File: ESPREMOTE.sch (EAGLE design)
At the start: 37 parts, among them IC1 ESP12SMT, IC2 LD111733, J1 DC_2_1MM, Q1 2N7002, Q2 2N7002, Q3 2N7002, Q4 2N7002

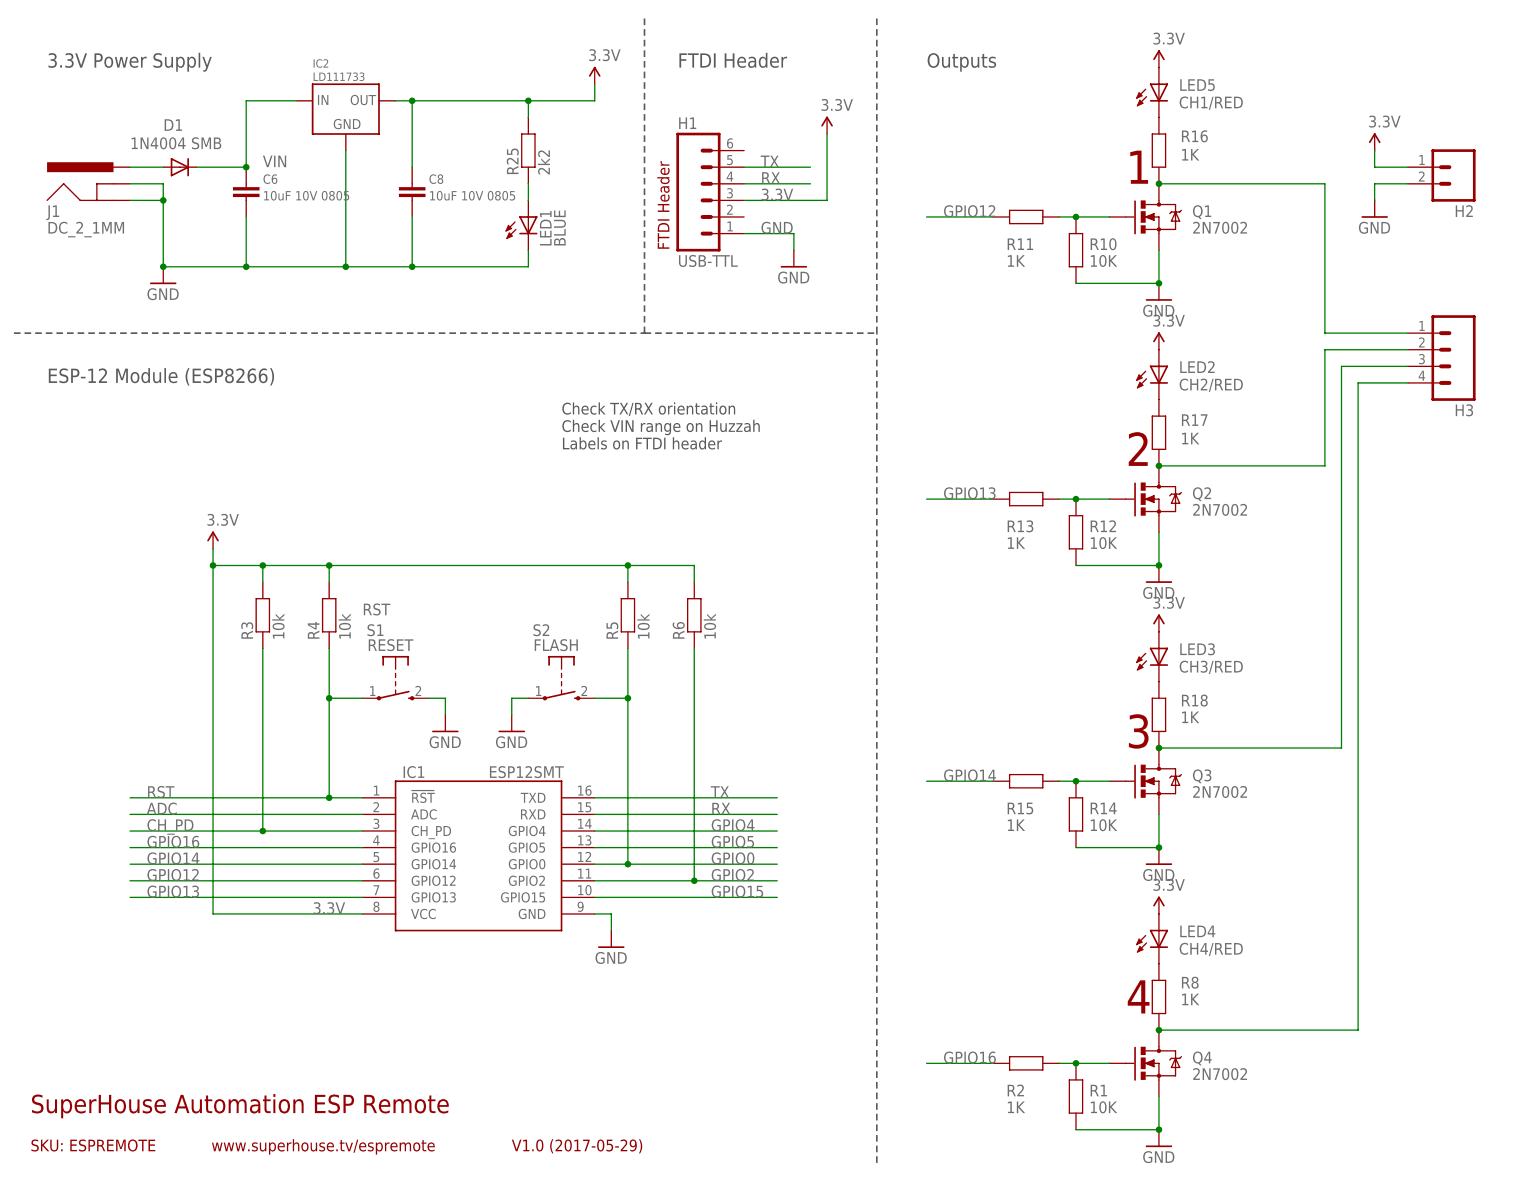
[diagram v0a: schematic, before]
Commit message: Finished schematic and routing for v1.0 release
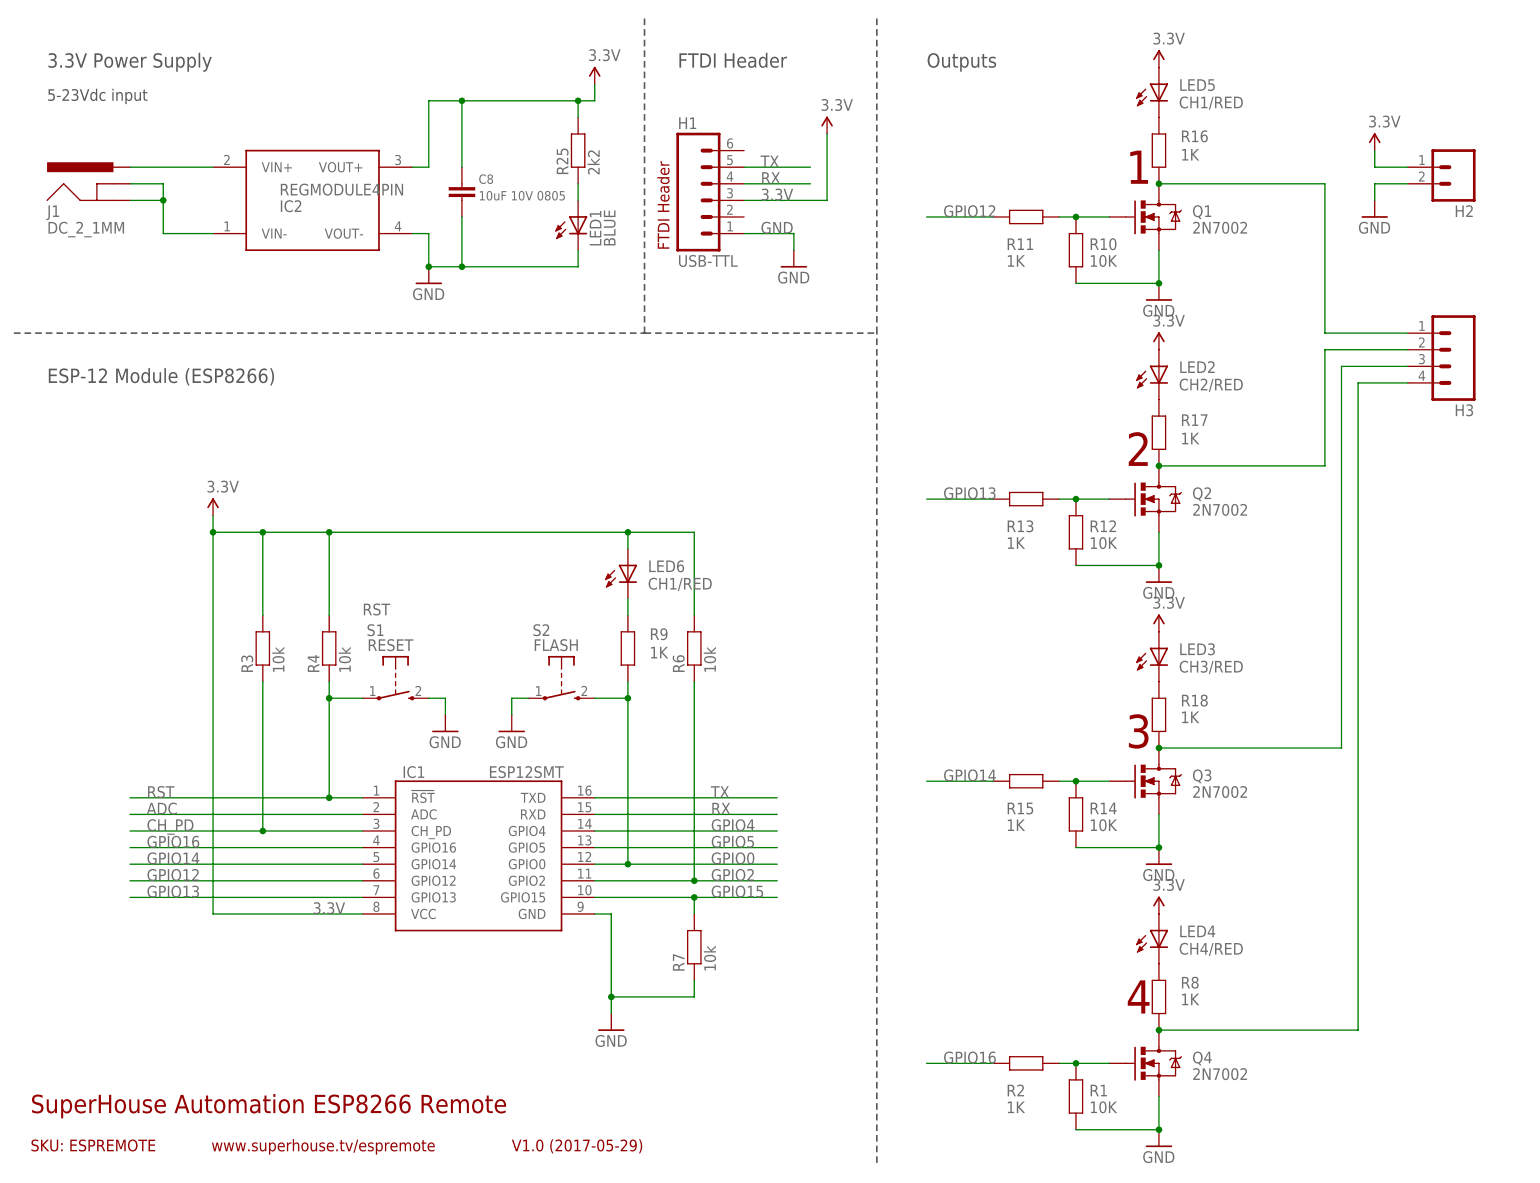
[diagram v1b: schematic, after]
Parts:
- removed C6: 10uF 10V 0805, freetronics-jon:C-EUC0805
- removed D1: 1N4004 SMB, freetronics:DIODESMB
- removed R5: 10k, freetronics-jon:RESISTOR0603
- added LED6: CH1/RED, freetronics-master-v1:LED0603
- added R7: 10k, freetronics-jon:RESISTOR0603
- added R9: 1K, freetronics-master-v1:RESISTOR0603
- IC2: value LD111733 -> REGMODULE4PIN; device freetronics-luke:LD1117-FIXED -> freetronics-jon:REGMODULE4PIN
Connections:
- removed net VIN: C6.1, D1.C, IC2.IN
- new net N$27: LED6.C, R9.1
- new net N$28: IC2.VIN-, J1.GND, J1.GNDBREAK
- net 3.3V: now also IC2.VOUT+, LED6.A; no longer IC2.OUT, R5.2
- net GND: now also IC2.VOUT-, R7.1; no longer C6.2, IC2.GND, J1.GND, J1.GNDBREAK
- net GPIO0: now also R9.2; no longer R5.1
- net GPIO15: now also R7.2
- net N$8: now also IC2.VIN+; no longer D1.A
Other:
- note added: "5-23Vdc input"
- note added: "SuperHouse Automation ESP8266 Remote"
- note removed: "Check TX/RX orientation Check VIN range on Huzzah Labels on FTDI header"
- note removed: "SOT-223"
- note removed: "SuperHouse Automation ESP Remote"
- moved on the sheet: C8, LED1, R25, R3, R4, R6

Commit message: Final silkscreen and label improvements for v1.0 release
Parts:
- LED6: value CH1/RED -> GREEN
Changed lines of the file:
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@@
 <part name="P+10" library="freetronics-original" deviceset="3.3V" device=""/>
 <part name="R7" library="freetronics-jon" deviceset="RESISTOR" device="0603" value="10k"/>
-<part name="LED6" library="freetronics-master-v1" deviceset="LED" device="0603" value="CH1/RED"/>
+<part name="LED6" library="freetronics-master-v1" deviceset="LED" device="0603" value="GREEN"/>
 <part name="R9" library="freetronics-master-v1" deviceset="RESISTOR" device="0603" value="1K"/>
 <part name="IC2" library="freetronics-jon" deviceset="REGMODULE4PIN" device=""/>

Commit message: Added output info to silkscreen
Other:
- note added: "Output 1: GPIO12 Output 2: GPIO13 Output 3: GPIO14 Output 4: GPIO16"
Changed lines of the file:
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@@
 <text x="106.68" y="172.72" size="2.1844" layer="97" font="vector" ratio="15">FTDI Header</text>
 <text x="10.16" y="167.64" size="1.778" layer="97" font="vector" ratio="10">5-23Vdc input</text>
+<text x="104.14" y="114.3" size="1.778" layer="97" font="vector" ratio="10">Output 1: GPIO12
+Output 2: GPIO13
+Output 3: GPIO14
+Output 4: GPIO16</text>
 </plain>
 <instances>
@@
 </schematic>
 </drawing>
+<compatibility>
+<note version="6.3" minversion="6.2.2" severity="warning">
+Since Version 6.2.2 text objects can contain more than one line,
+which will not be processed correctly with this version.
+</note>
+</compatibility>
 </eagle>

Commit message: Changed output 4 from GPIO16 to GPIO4
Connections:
- net GPIO16: no longer R2.2
- net GPIO4: now also R2.2
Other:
- note added: "Output 1: GPIO12 Output 2: GPIO13 Output 3: GPIO14 Output 4: GPIO4"
- note added: "V2.0 (2017-07-29)"
- note removed: "Output 1: GPIO12 Output 2: GPIO13 Output 3: GPIO14 Output 4: GPIO16"
- note removed: "V1.0 (2017-05-29)"
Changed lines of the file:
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@@
 <text x="7.62" y="6.858" size="1.778" layer="94">SKU: ESPREMOTE</text>
 <text x="7.62" y="12.7" size="2.794" layer="94">SuperHouse Automation ESP8266 Remote</text>
-<text x="81.28" y="6.858" size="1.778" layer="94">V1.0 (2017-05-29)</text>
+<text x="81.28" y="6.858" size="1.778" layer="94">V2.0 (2017-07-29)</text>
 <text x="35.306" y="6.858" size="1.778" layer="94">www.superhouse.tv/espremote</text>
 <frame x1="5.08" y1="5.08" x2="109.22" y2="17.78" columns="0" rows="0" layer="94" border-left="no" border-top="no" border-right="no" border-bottom="no"/>
@@
 Output 2: GPIO13
 Output 3: GPIO14
-Output 4: GPIO16</text>
+Output 4: GPIO4</text>
 </plain>
 <instances>
@@
 <label x="111.76" y="55.88" size="1.778" layer="95"/>
 </segment>
+<segment>
+<pinref part="R2" gate="G$1" pin="2"/>
+<wire x1="154.94" y1="20.32" x2="144.78" y2="20.32" width="0.1524" layer="91"/>
+<label x="147.32" y="20.32" size="1.778" layer="95"/>
+</segment>
 </net>
 <net name="GPIO14" class="0">
@@
 <label x="25.4" y="53.34" size="1.778" layer="95"/>
 </segment>
-<segment>
-<pinref part="R2" gate="G$1" pin="2"/>
-<wire x1="154.94" y1="20.32" x2="144.78" y2="20.32" width="0.1524" layer="91"/>
-<label x="147.32" y="20.32" size="1.778" layer="95"/>
-</segment>
-</net>
+</net>

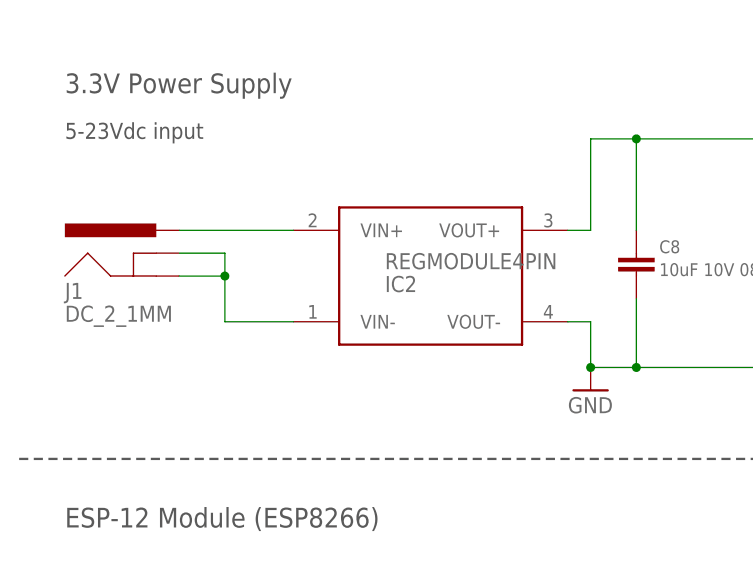
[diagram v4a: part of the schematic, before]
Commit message: Replaced 2.1mm DC jack and switchmode reg with USB socket and linear reg
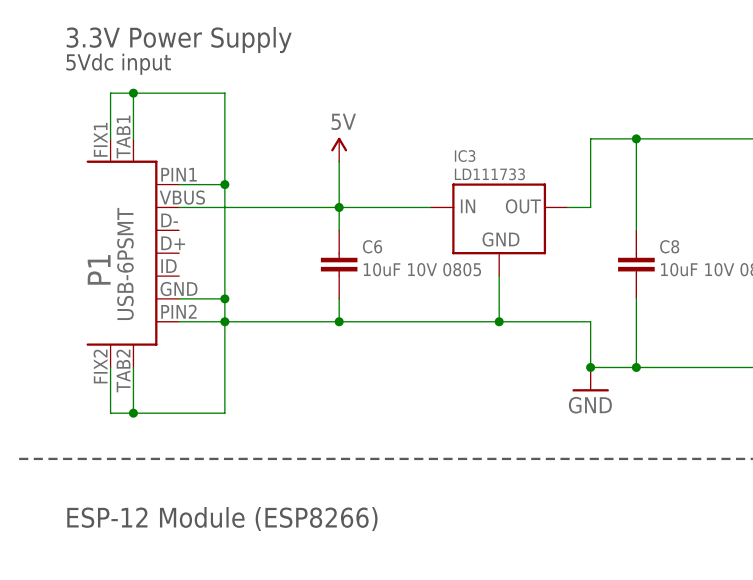
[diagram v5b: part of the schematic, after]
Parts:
- removed IC2: REGMODULE4PIN, freetronics-jon:REGMODULE4PIN
- removed J1: DC_2_1MM, freetronics:POWER_JACKPTH
- added C6: 10uF 10V 0805, freetronics-jon:C-EUC0805
- added IC3: LD111733, freetronics-luke:LD1117-FIXED
- added P1: USB-6PSMT, freetronics-jon:USB-6PSMT
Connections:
- removed net N$28: IC2.VIN-, J1.GND, J1.GNDBREAK
- removed net N$8: IC2.VIN+, J1.PWR
- new net 5V: C6.1, IC3.IN, P1.VBUS
- net 3.3V: now also IC3.OUT; no longer IC2.VOUT+
- net GND: now also C6.2, IC3.GND, P1.FIX1, P1.FIX2, P1.GND, P1.PIN1, P1.PIN2, P1.TAB1, P1.TAB2; no longer IC2.VOUT-
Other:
- note added: "5Vdc input"
- note added: "SOT-223"
- note removed: "5-23Vdc input"

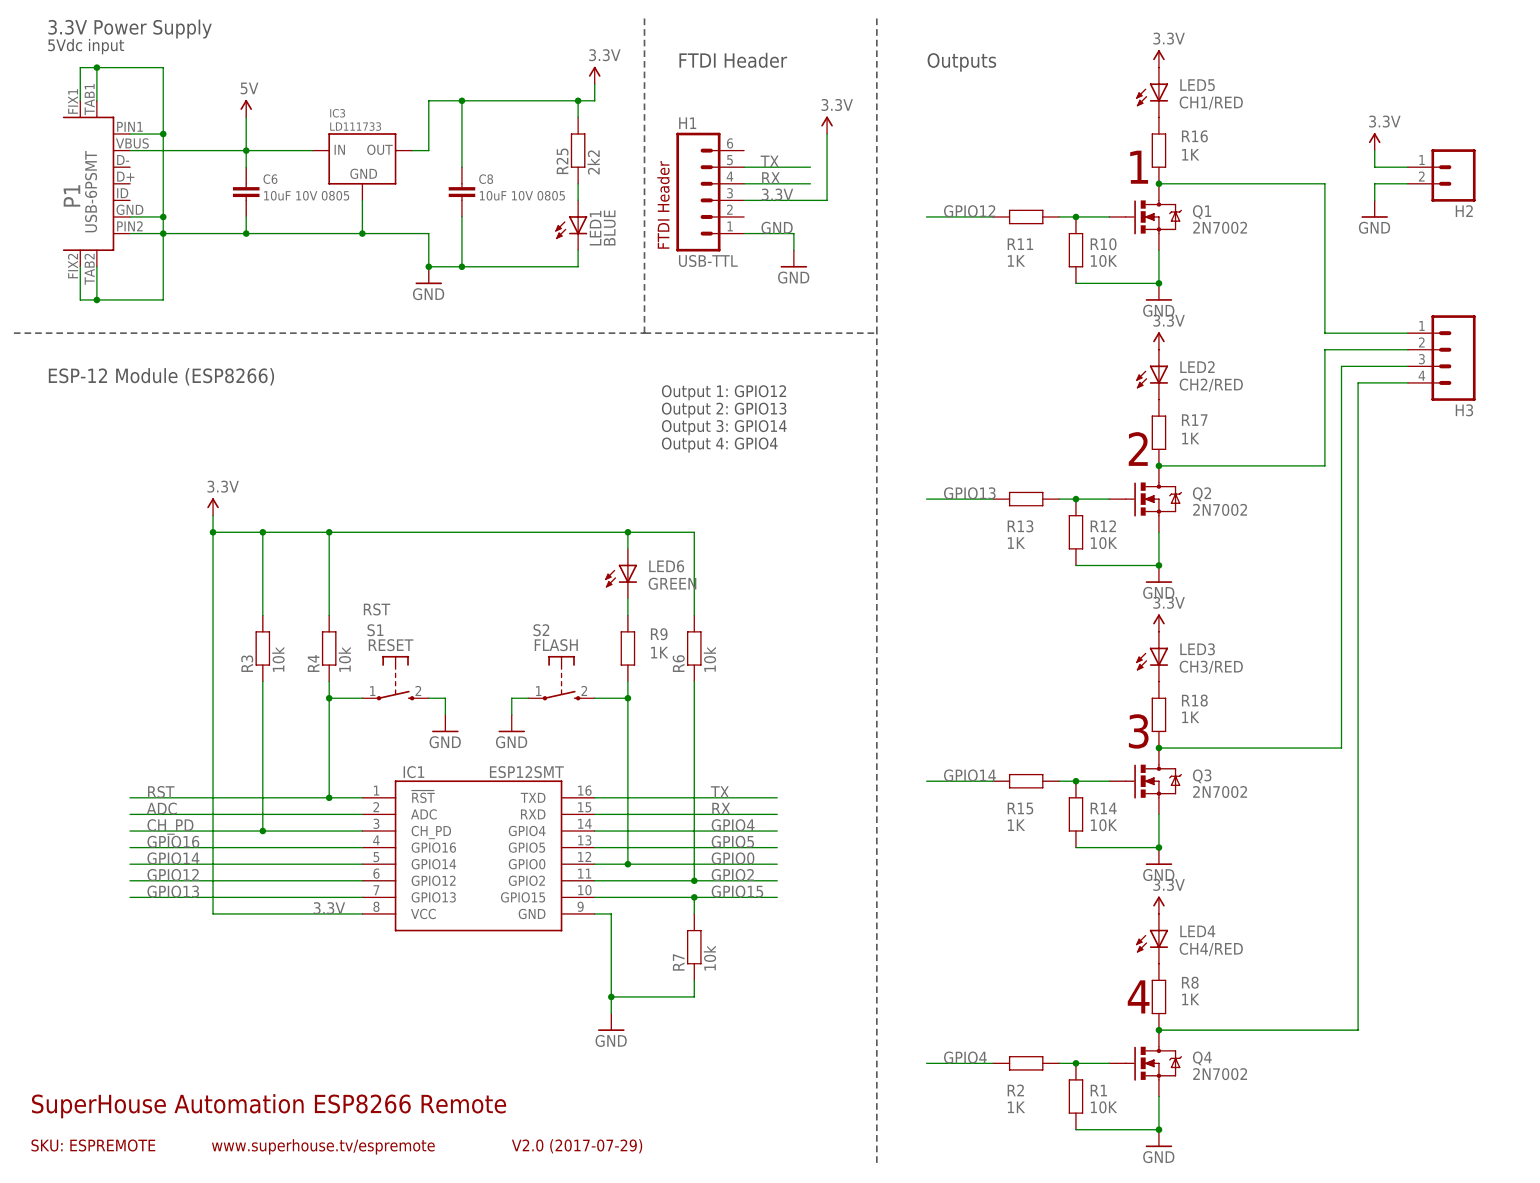
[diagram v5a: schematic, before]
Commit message: Replaced crappy SMPS with linear reg and micro USB socket
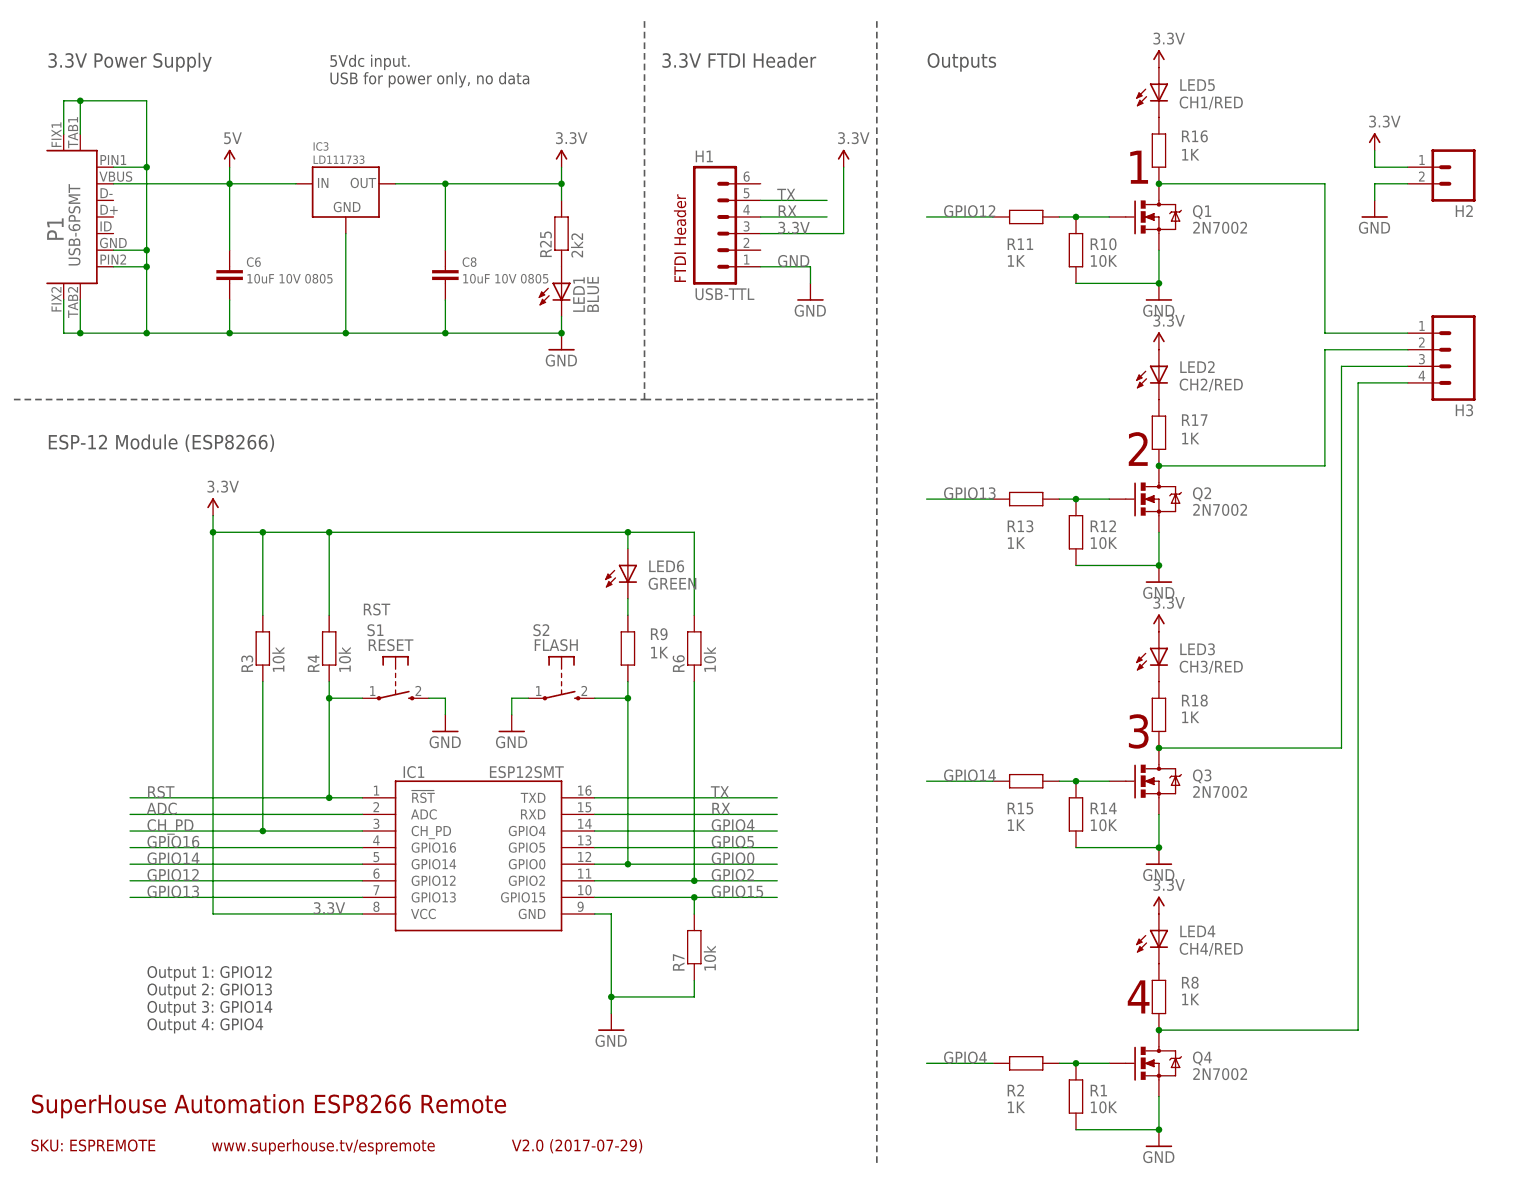
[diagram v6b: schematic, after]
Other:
- note added: "3.3V FTDI Header"
- note added: "5Vdc input. USB for power only, no data"
- note removed: "5Vdc input"
- moved on the sheet: C6, C8, H1, IC3, LED1, P1, R25
